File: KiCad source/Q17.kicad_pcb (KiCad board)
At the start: 2 copper layers, 156.2 x 58.3 mm, 84 parts, among them J1 Input, J2 Speaker, J3 Screw_Terminal_01x03, Q1 IRF610, Q10 2SA970, Q11 BS250, Q12 2SC2240, Q13 IRF610, Q14 IRF9610, Q15 FQA46N15, Q16 FQA36P15, Q2 2SA970, Q3 2SC2240, Q4 IRF9610, Q5 FQP3P20, Q6 FQP3N30, Q7 2SC2240, Q8 2N7000, Q9 BS250, U1 OPA1641

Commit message: Add files via upload
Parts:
- removed REF**: KiCad-Logo_5mm_SilkScreen, Symbol:KiCad-Logo_5mm_SilkScreen
- L1: footprint inductor:L -> L:L_new
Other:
- board text removed: "Q17"

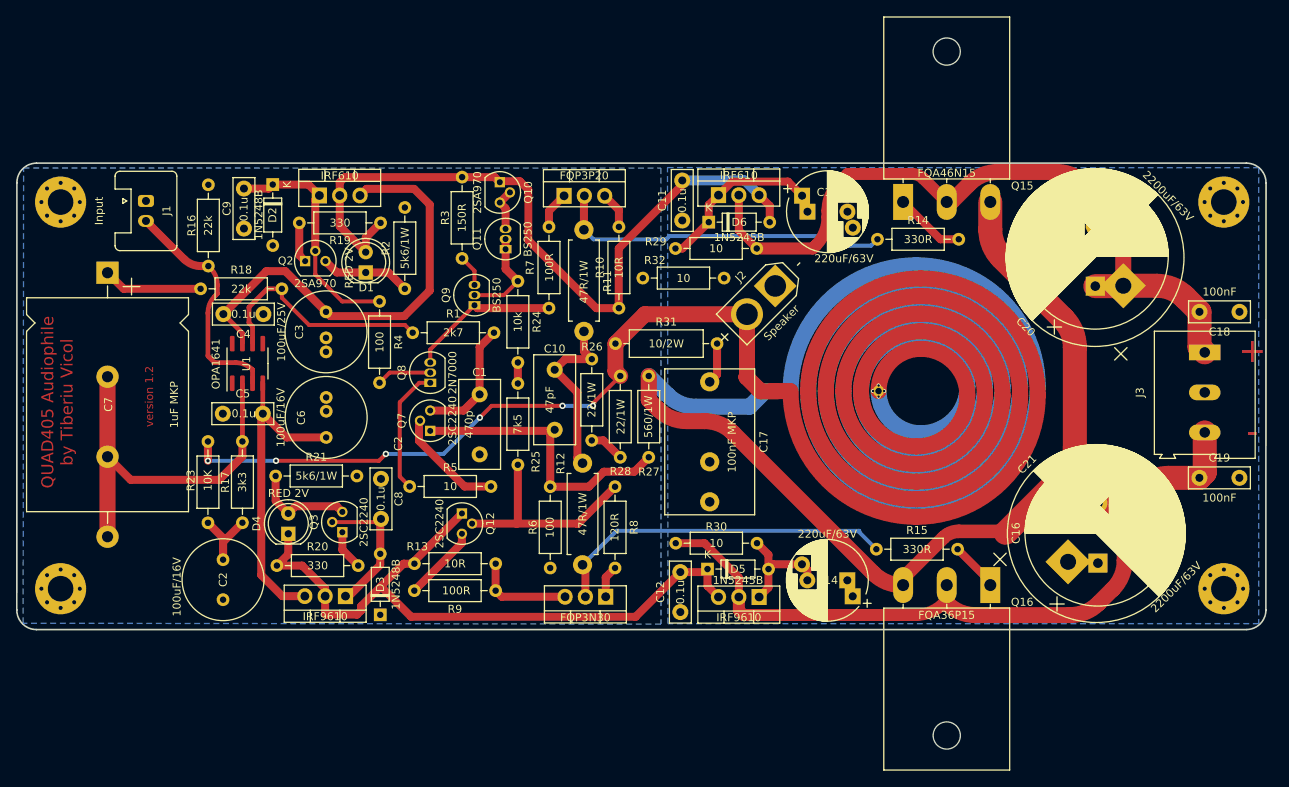
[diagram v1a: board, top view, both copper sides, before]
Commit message: BS250 footprint changed for Diodes
There are at least two footprints for BS250 that may be confusing. 
Changes also include:
Smooth traces. 
Reposition of few parts.
Some traces have been enlarged.
Coil was adjusted to take account for other traces with parasitic inductances.
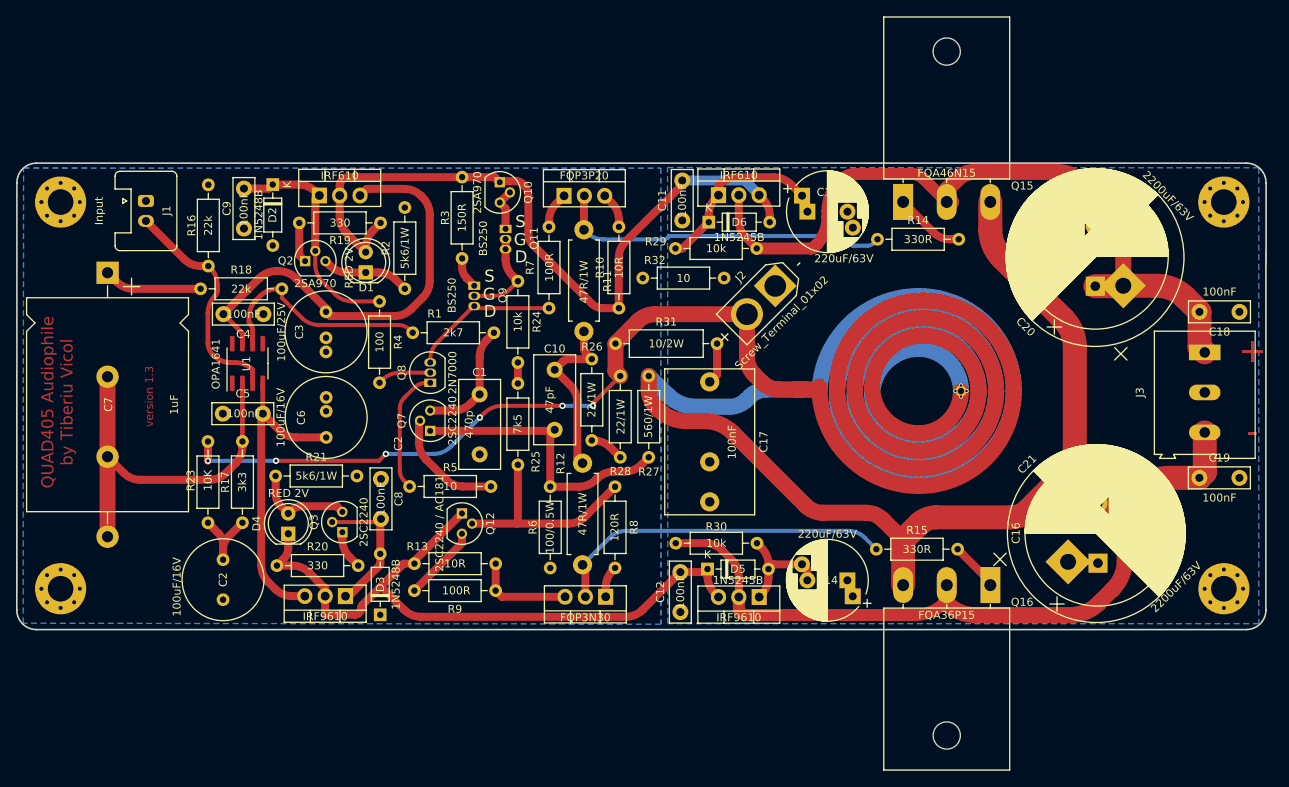
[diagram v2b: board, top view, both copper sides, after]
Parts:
- C11, C12, C4, C5, C8, C9: value 0.1u -> 100nF
- C17: value 100nF MKP -> 100nF
- C7: value 1uF MKP -> 1uF
- J2: value Speaker -> Screw_Terminal_01x02
- Q11, Q9: footprint Package_TO_SOT_THT:TO-92_Inline -> Package_TO_SOT_THT:TO-92L_Inline
- Q12: value 2SC2240 -> 2SC2240 / AC181
- R29, R30: value 10 -> 10k
- R6: value 100 -> 100/0.5W
- moved Q11 2.54 mm to (134.6, 75.8), turned to -90 degrees
- moved Q9 2.44 mm to (130.7, 82.9), turned to -90 degrees
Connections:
- J2 pad 1: GNDPWR -> Net-(J2-Pad1)
- J2 pad 2: Net-(J2-Pad1) -> GNDPWR
- Q11 pad 1: Net-(R24-Pad1) -> Net-(Q10-Pad2)
- Q11 pad 2: Net-(R24-Pad1) -> Net-(Q11-Pad2)
- Q11 pad 3: Net-(Q10-Pad2) -> Net-(Q11-Pad2)
- Q9 pad 1: Net-(Q8-Pad3) -> Net-(Q9-Pad1)
- Q9 pad 2: Net-(R24-Pad1) -> Net-(Q11-Pad2)
- Q9 pad 3: Net-(R3-Pad2) -> Net-(Q8-Pad3)
- R24 pad 1: Net-(R24-Pad1) -> Net-(Q11-Pad2)
- R3 pad 2: Net-(R3-Pad2) -> Net-(Q9-Pad1)
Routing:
- net Net-(R24-Pad1): track 12.3 -> 0.00 mm
- net Net-(Q11-Pad2): track 0.00 -> 12.0 mm
- net Net-(L1-Pad2): track 126.1 -> 131.5 mm
- net Net-(R3-Pad2): track 4.02 -> 0.00 mm
- net Net-(Q9-Pad1): track 0.00 -> 4.00 mm
- net Net-(J2-Pad1): track 93.4 -> 95.0 mm
- net Net-(C15-Pad1): track 91.9 -> 93.2 mm
- net Net-(C11-Pad2): track 94.1 -> 93.1 mm
- net Net-(J1-Pad2): track 29.7 -> 29.0 mm
- net Net-(C12-Pad2): track 86.8 -> 86.0 mm
- net Net-(C13-Pad1): track 21.3 -> 22.0 mm
- net Net-(C3-Pad1): track 57.0 -> 56.4 mm
- net Net-(R1-Pad1): track 29.1 -> 28.5 mm
- net Net-(Q7-Pad2): track 13.8 -> 14.4 mm
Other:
- board text added: "D"
- board text added: "G"
- board text added: "S"
- board text added: "version 1.3"
- board text removed: "version 1.2"

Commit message: Add files via upload
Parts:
- moved Q6 4.10 mm to (147.0, 125.9)
- moved Q5 4.09 mm to (141.9, 67.6)
- moved R10 3.00 mm to (148.8, 82.7)
- moved R7 2.95 mm to (140.0, 82.8)
- moved R11 2.92 mm to (144.4, 73.0)
- moved R12 2.49 mm to (144.5, 107.6)
- moved R6 2.49 mm to (140.4, 110.5)
- moved R8 2.49 mm to (148.5, 110.5)
- moved Q15 0.06 mm to (184.3, 72.4)
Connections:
- J2 pad 1: Net-(J2-Pad1) -> GNDPWR
- J2 pad 2: GNDPWR -> Net-(J2-Pad1)
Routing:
- net Net-(C10-Pad1): track 21.9 -> 30.4 mm
- net Net-(C11-Pad2): track 93.1 -> 86.3 mm
- net Net-(Q6-Pad2): track 42.8 -> 46.4 mm
- net Net-(C10-Pad2): track 36.4 -> 39.8 mm
- net Net-(Q5-Pad2): track 42.0 -> 45.2 mm
- net Net-(C12-Pad2): track 86.0 -> 88.1 mm
- net Net-(Q8-Pad3): track 18.7 -> 20.0 mm
- net Net-(Q12-Pad2): track 27.0 -> 27.9 mm
- net Net-(Q6-Pad1): track 3.94 -> 4.59 mm
- net Net-(Q6-Pad3): track 12.4 -> 13.0 mm

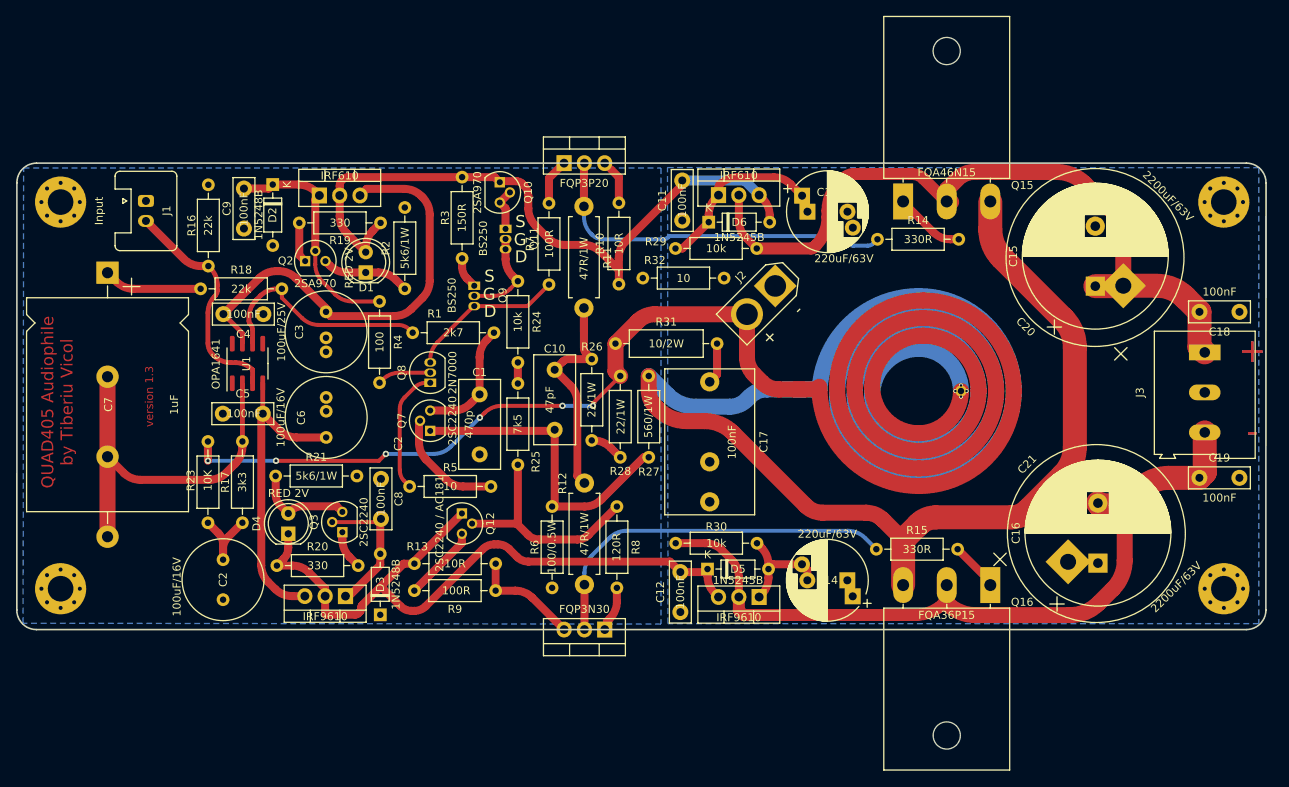
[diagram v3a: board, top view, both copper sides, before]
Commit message: Lot of DRC errors have been cleared
There are few DRC errors left due castellated holes and inductor.
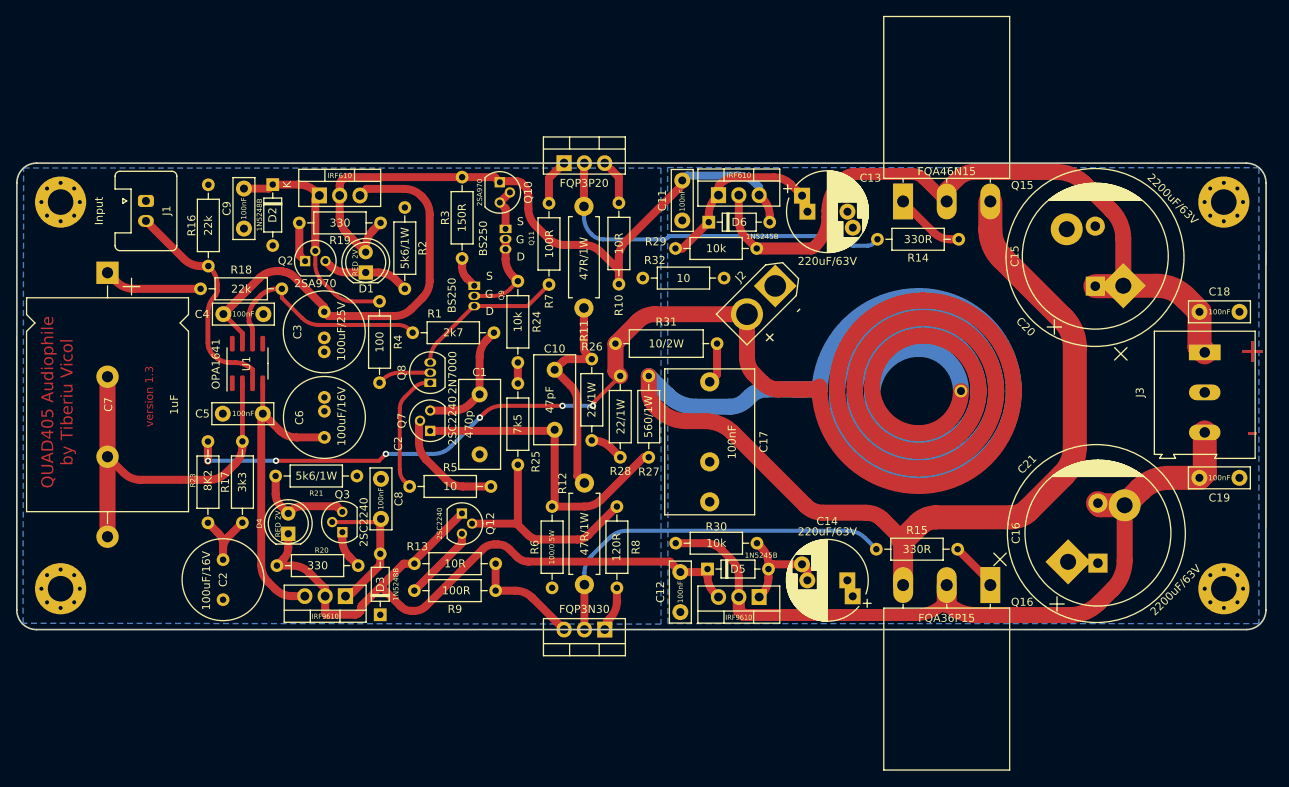
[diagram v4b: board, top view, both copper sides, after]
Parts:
- Q12: value 2SC2240 / AC181 -> 2SC2240
- R23: value 10K -> 8K2
- moved C3 0.22 mm to (112.0, 86.2)
- moved C6 0.22 mm to (112.0, 96.9)
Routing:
- net Net-(C16-Pad2): track 98.2 -> 96.3 mm
- net Net-(L1-Pad2): track 131.5 -> 129.7 mm
- net Net-(C11-Pad2): track 86.3 -> 87.2 mm
- net Net-(Q16-Pad1): track 6.75 -> 6.18 mm
- net Net-(C15-Pad1): track 93.2 -> 92.7 mm
- net (no net): vias 4 -> 0
